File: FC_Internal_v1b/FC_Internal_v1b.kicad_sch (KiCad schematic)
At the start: 101 parts, among them IC1 RP2040_QFN56, IC2 AZ1117CH-3.3TRG1, IC3 RV-3028-C7_32.768kHz_1ppm_TA_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, J1 Conn_ARM_JTAG_SWD_10, J10 BM04B-SRSS-TB(LF)(SN), J11 BM04B-SRSS-TB(LF)(SN), J12 BM04B-SRSS-TB(LF)(SN), J13 Breakout, J15 Battery, J15 Breakout, J16 Debug, J2 FC to EPS Connector, J3 Life Makes Lemonade, J4 Molex 503398-1892, J5 BM04B-SRSS-TB(LF)(SN), J6 Conn_Coaxial, J7 Breakout, J8 USB_B_Micro, J9 BM04B-SRSS-TB(LF)(SN), SW1 KMR2, SW2 KMR2, U10 AP3602AKTR-G1, U3 MAX706RESA, U4 RFM98PW, U5 RFM9xBreakout, U6 W25Q128JV, U7 LSM6DSOTR, U8 LSM303AGRTR, U9 MCP25625-E/ML, Y1 12MHZ, Y3 16MHZ 12 pf

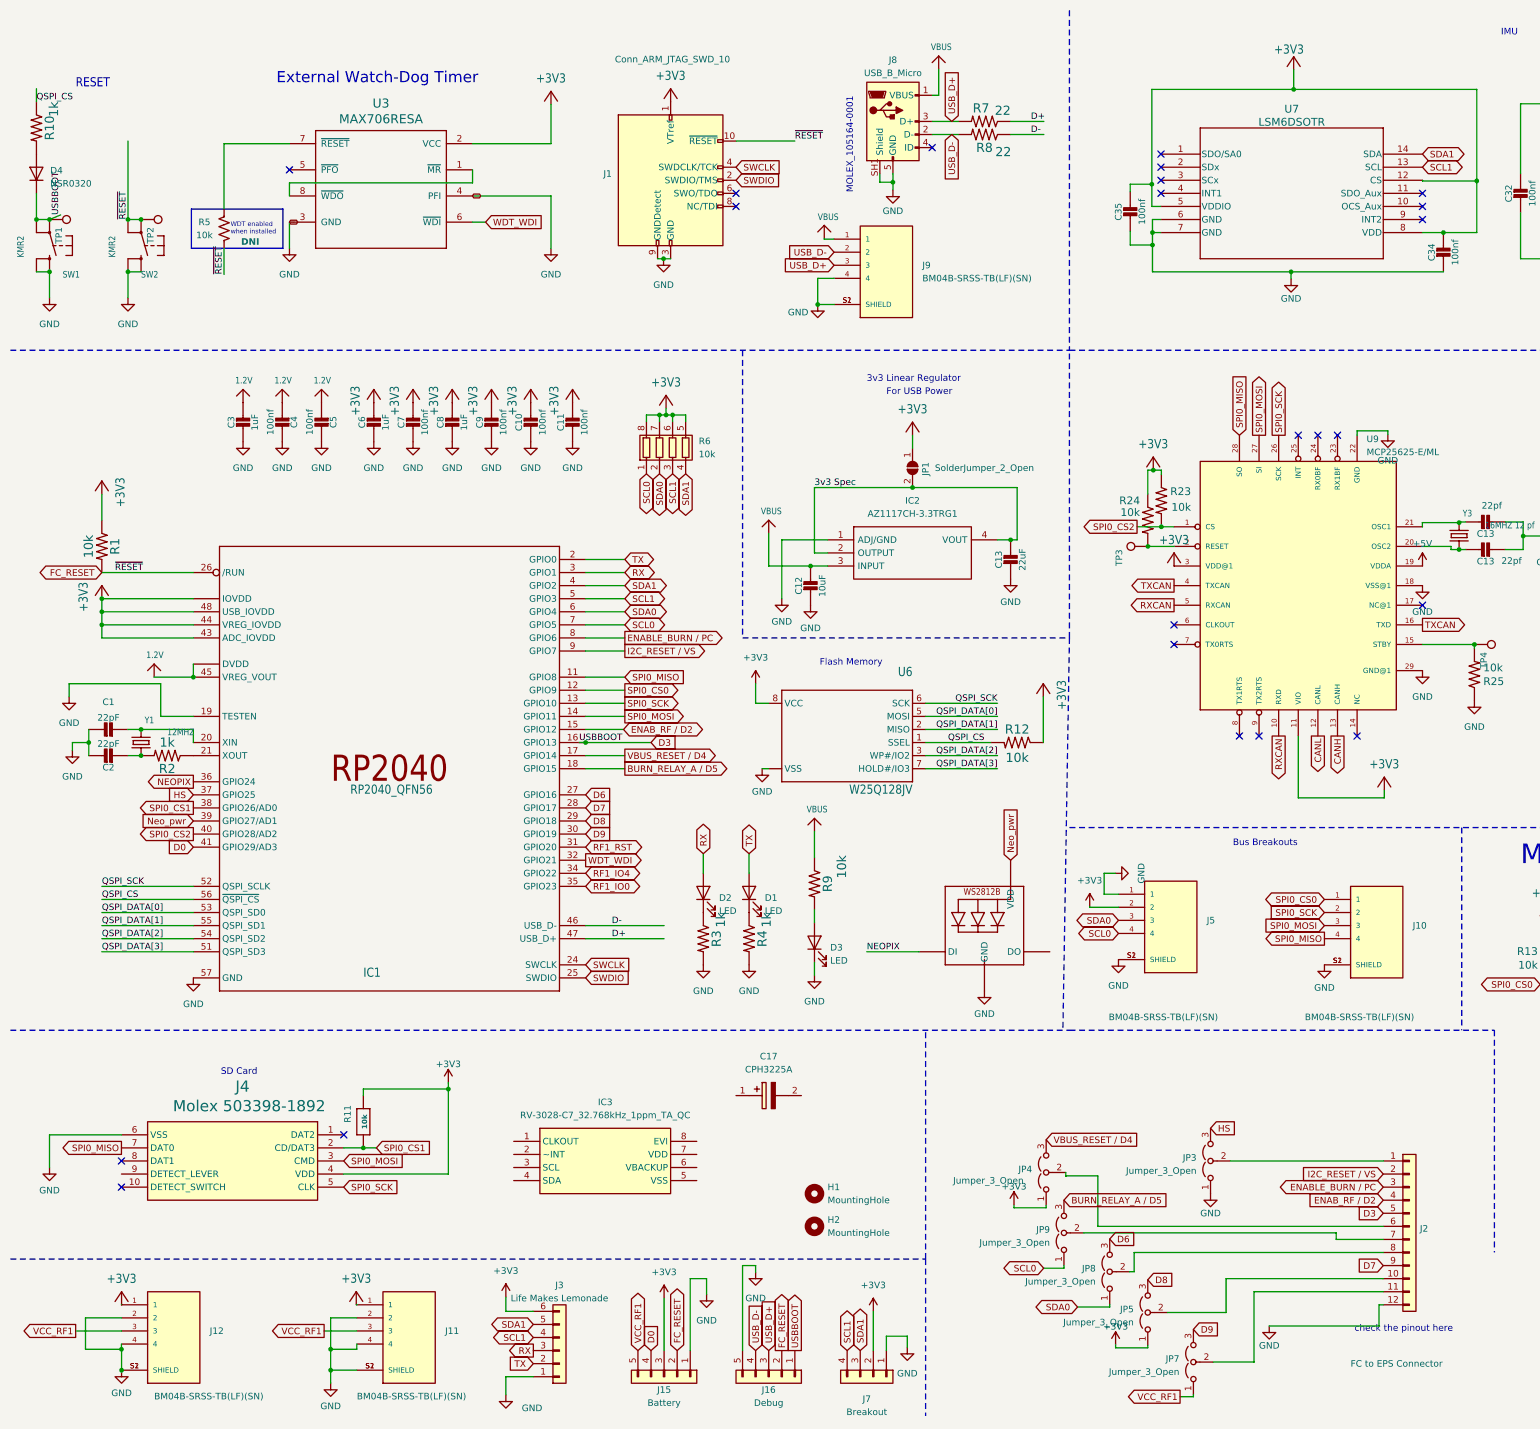
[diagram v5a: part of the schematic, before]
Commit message: Real Time Clock Implemented
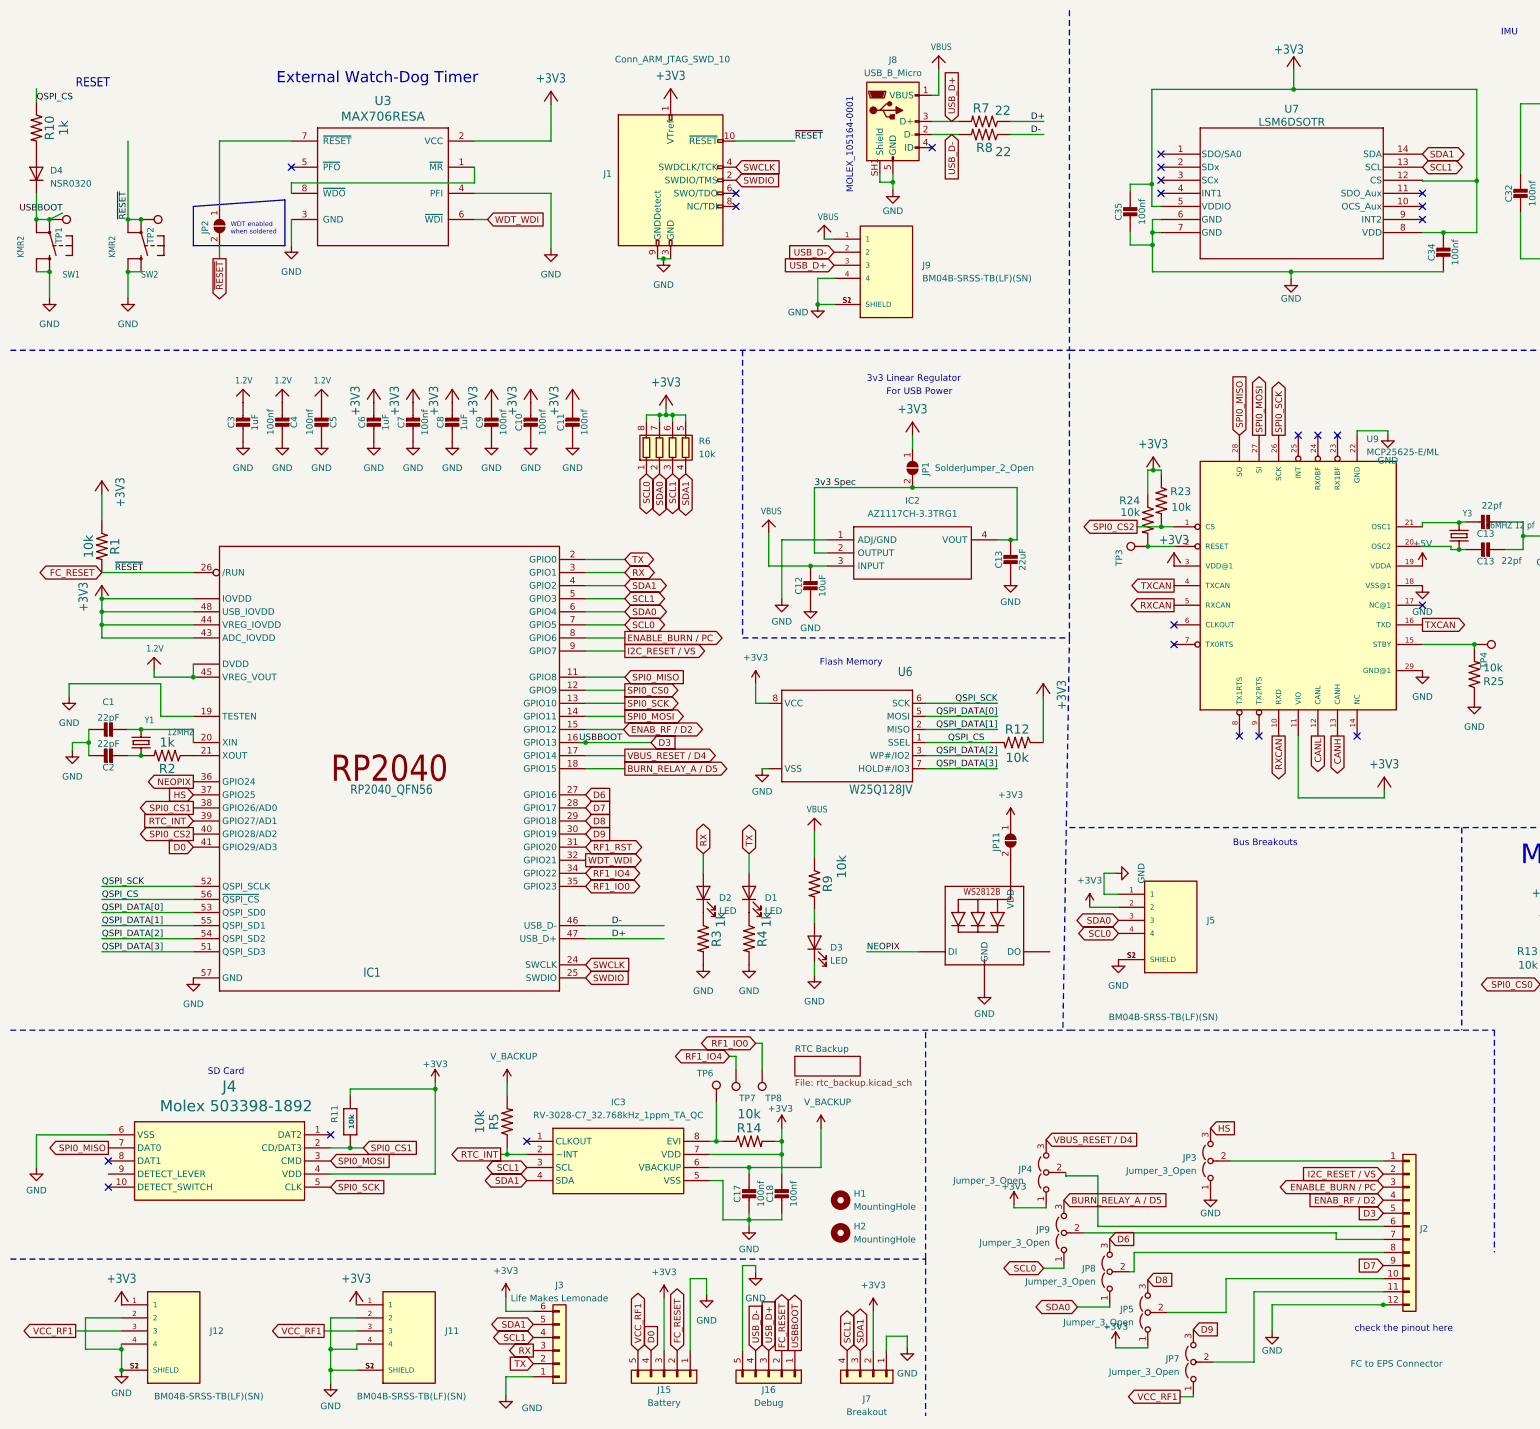
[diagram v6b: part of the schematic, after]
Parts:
- removed C17: CPH3225A, SuperCap:CPH3225A, symbol CPH3225A:CPH3225A
- removed J10: BM04B-SRSS-TB(LF)(SN), FC_DEV_BOARD:JST_BM04B-SRSS-TB(LF)(SN), symbol BM04B-SRSS-TB_LF__SN_:BM04B-SRSS-TB(LF)(SN)
- removed R5: 10k, Resistor_SMD:R_0603_1608Metric, symbol Device:R_US
- added C17, C18: 100nf, Capacitor_SMD:C_0402_1005Metric, symbol Adafruit ItsyBitsy RP2040-eagle-import:CAP_CERAMIC_0402NO
- added JP11, JP2: SolderJumper_2_Open, Jumper:SolderJumper-2_P1.3mm_Open_RoundedPad1.0x1.5mm, symbol Jumper:SolderJumper_2_Open
- added R14, R5: 10k, Resistor_SMD:R_0603_1608Metric, symbol mainboard:RESISTOR0603
- added TP6, TP7, TP8: RESET, TestPoint:TestPoint_Loop_D1.80mm_Drill1.0mm_Beaded, symbol Connector:TestPoint
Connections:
- net +3V3: now also IC3.7 (VDD), C18.1, JP11.1 (A), R14.2
- net FC_RESET: now also JP2.2 (B)
- net GND: now also IC3.5 (VSS), C17.2, C18.2
- net RF1_IO0: now also TP8.1
- net RF1_IO4: now also TP7.1
- net SCL1: now also IC3.3 (SCL)
- net SDA1: now also IC3.4 (SDA)
- net RTC_INT: now reaches IC3.2 (~INT)
- net RTC_INT: now also IC1.39 (GPIO27/AD1), R5.1
- net V_BACKUP: now reaches IC3.6 (VBACKUP)
- net V_BACKUP: now also C17.1, R5.2
- net at IC3.8 (EVI): now also R14.1, TP6.1
- net at U3.7 (~{RESET}): now also JP2.1 (A)
- net Neo_pwr: no longer names the net of LED1.1 (VDD)
- net Neo_pwr: now also JP11.2 (B); no longer IC1.39 (GPIO27/AD1)
- no-connect marks 34 -> 35
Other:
- added sheet RTC Backup (rtc_backup.kicad_sch)
- note added: "WDT enabled when soldered"
- note removed: "WDT enabled when installed"
- moved on the sheet: H1, H2, IC3, J4, R11, U3
